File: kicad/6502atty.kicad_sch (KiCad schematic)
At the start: 30 parts, among them J10 Conn_01x04_Pin, J11 Conn_01x03_Pin, J12 Conn_01x02_Pin, J2 Conn_01x02_Pin, J8 Conn_01x03_Pin, U6 27C128, U7 KM62256CLP

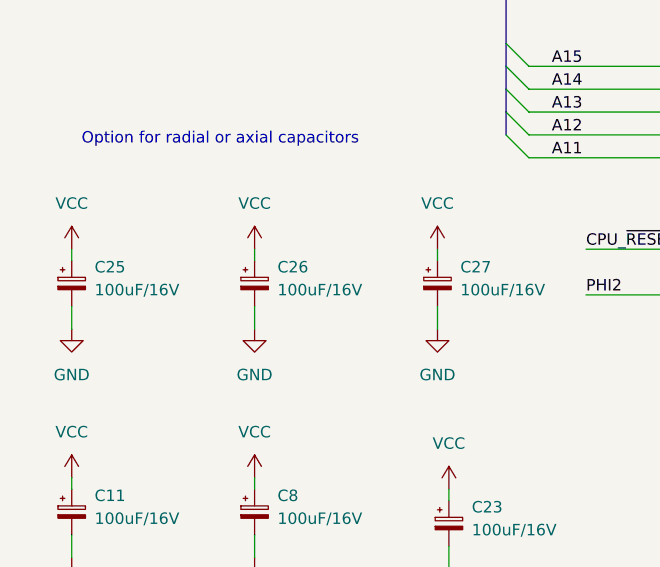
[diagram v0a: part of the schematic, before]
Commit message: pcb: move around stuff to make pcb smaller
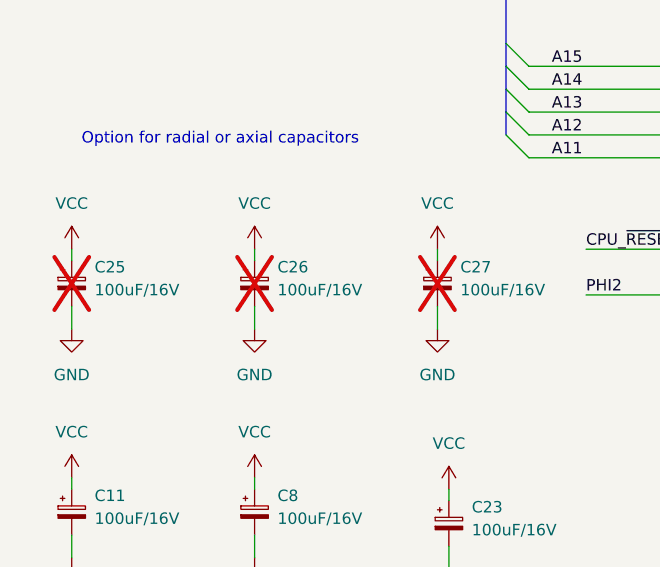
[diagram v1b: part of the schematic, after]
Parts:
- C25, C26, C27: now not fitted
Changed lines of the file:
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@@
 		(in_bom yes)
 		(on_board yes)
-		(dnp no)
+		(dnp yes)
 		(fields_autoplaced yes)
 		(property "Reference" "C26"
@@
 		(in_bom yes)
 		(on_board yes)
-		(dnp no)
+		(dnp yes)
 		(fields_autoplaced yes)
 		(property "Reference" "C27"
@@
 		(in_bom yes)
 		(on_board yes)
-		(dnp no)
+		(dnp yes)
 		(fields_autoplaced yes)
 		(property "Reference" "C25"

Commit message: start of rev3, reduce x-size, leds consistent
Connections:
- net GND: now also R37.2; no longer D2.1 (K)
- net VCC: now also D2.2 (A); no longer R37.1
- new net: D2.1 (K), R37.1
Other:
- moved on the sheet: R37
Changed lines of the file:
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@@
 	(wire
 		(pts
+			(xy 234.95 105.41) (xy 234.95 104.14)
+		)
+		(stroke
+			(width 0)
+			(type default)
+		)
+	)
+	(wire
+		(pts
 			(xy 189.23 53.34) (xy 198.12 53.34)
 		)
@@
 	(wire
 		(pts
+			(xy 234.95 113.03) (xy 234.95 115.57)
+		)
+		(stroke
+			(width 0)
+			(type default)
+		)
+	)
+	(wire
+		(pts
 			(xy 260.35 34.29) (xy 260.35 33.02)
 		)
@@
 		)
 	)
+	(wire
+		(pts
+			(xy 234.95 90.17) (xy 234.95 99.06)
+		)
+		(stroke
+			(width 0)
+			(type default)
+		)
+	)
 	(bus
 		(pts
@@
 		)
 	)
-	(wire
-		(pts
-			(xy 234.95 97.79) (xy 234.95 99.06)
-		)
-		(stroke
-			(width 0)
-			(type default)
-		)
-	)
 	(bus
 		(pts
@@
 	(wire
 		(pts
-			(xy 234.95 104.14) (xy 234.95 106.68)
-		)
-		(stroke
-			(width 0)
-			(type default)
-		)
-	)
-	(wire
-		(pts
 			(xy 24.13 66.04) (xy 38.1 66.04)
 		)
@@
 	(symbol
 		(lib_id "power:GND")
-		(at 234.95 106.68 0)
+		(at 234.95 115.57 0)
 		(unit 1)
 		(exclude_from_sim no)
@@
 		(dnp no)
 		(property "Reference" "#PWR0102"
-			(at 234.95 113.03 0)
+			(at 234.95 121.92 0)
 			(effects
 				(font
@@
 		)
 		(property "Value" "GND"
-			(at 234.95 111.76 0)
+			(at 234.95 120.65 0)
 			(effects
 				(font
@@
 		)
 		(property "Footprint" ""
-			(at 234.95 106.68 0)
+			(at 234.95 115.57 0)
 			(effects
 				(font
@@
 		)
 		(property "Datasheet" ""
-			(at 234.95 106.68 0)
+			(at 234.95 115.57 0)
 			(effects
 				(font
@@
 		)
 		(property "Description" "Power symbol creates a global label with name \"GND\" , ground"
-			(at 234.95 106.68 0)
+			(at 234.95 115.57 0)
 			(effects
 				(font
@@
 	(symbol
 		(lib_id "Device:R")
-		(at 234.95 93.98 0)
+		(at 234.95 109.22 0)
 		(unit 1)
 		(exclude_from_sim no)
@@
 		(fields_autoplaced yes)
 		(property "Reference" "R37"
-			(at 237.49 92.7099 0)
+			(at 237.49 107.9499 0)
 			(effects
 				(font
@@
 		)
 		(property "Value" "1K"
-			(at 237.49 95.2499 0)
+			(at 237.49 110.4899 0)
 			(effects
 				(font
@@
 		)
 		(property "Footprint" "Resistor_THT:R_Axial_DIN0207_L6.3mm_D2.5mm_P10.16mm_Horizontal"
-			(at 233.172 93.98 90)
+			(at 233.172 109.22 90)
 			(effects
 				(font
@@
 		)
 		(property "Datasheet" "~"
-			(at 234.95 93.98 0)
+			(at 234.95 109.22 0)
 			(effects
 				(font
@@
 		)
 		(property "Description" "Resistor"
-			(at 234.95 93.98 0)
+			(at 234.95 109.22 0)
 			(effects
 				(font

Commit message: updates for moving pcb stuff around
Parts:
- removed J8: Conn_01x03_Pin, Connector_PinHeader_2.54mm:PinHeader_1x03_P2.54mm_Vertical, symbol Connector:Conn_01x03_Pin
- added JP1: A13-Sel, symbol Jumper:SolderJumper_3_Bridged12
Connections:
- net A13: now also JP1.1 (A)
- net GND: now also JP1.3 (B)
- net ROM_A13: now also JP1.2 (C)
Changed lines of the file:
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@@
 	)
 	(bus_entry
-		(at 152.4 104.14)
+		(at 152.4 92.71)
 		(size -2.54 2.54)
 		(stroke
@@
 		)
 	)
+	(bus
+		(pts
+			(xy 152.4 97.79) (xy 152.4 100.33)
+		)
+		(stroke
+			(width 0)
+			(type default)
+		)
+	)
 	(wire
 		(pts
@@
 		)
 	)
-	(bus
-		(pts
-			(xy 152.4 95.25) (xy 152.4 97.79)
-		)
-		(stroke
-			(width 0)
-			(type default)
-		)
-	)
 	(wire
 		(pts
@@
 		)
 	)
-	(bus
-		(pts
-			(xy 152.4 97.79) (xy 152.4 100.33)
-		)
-		(stroke
-			(width 0)
-			(type default)
-		)
-	)
 	(wire
 		(pts
@@
 	(wire
 		(pts
-			(xy 148.59 130.81) (xy 148.59 109.22)
+			(xy 148.59 130.81) (xy 148.59 104.14)
 		)
 		(stroke
@@
 		)
 	)
+	(wire
+		(pts
+			(xy 142.24 95.25) (xy 149.86 95.25)
+		)
+		(stroke
+			(width 0)
+			(type default)
+		)
+	)
 	(bus
 		(pts
@@
 		)
 	)
-	(bus
-		(pts
-			(xy 152.4 104.14) (xy 152.4 105.41)
-		)
-		(stroke
-			(width 0)
-			(type default)
-		)
-	)
 	(wire
 		(pts
@@
 	(wire
 		(pts
+			(xy 142.24 110.49) (xy 142.24 109.22)
+		)
+		(stroke
+			(width 0)
+			(type default)
+		)
+	)
+	(wire
+		(pts
 			(xy 39.37 187.96) (xy 39.37 185.42)
 		)
@@
 	(bus
 		(pts
+			(xy 152.4 100.33) (xy 152.4 102.87)
+		)
+		(stroke
+			(width 0)
+			(type default)
+		)
+	)
+	(bus
+		(pts
 			(xy 152.4 50.8) (xy 152.4 53.34)
 		)
@@
 	(bus
 		(pts
-			(xy 152.4 100.33) (xy 152.4 102.87)
+			(xy 152.4 95.25) (xy 152.4 97.79)
+		)
+		(stroke
+			(width 0)
+			(type default)
+		)
+	)
+	(bus
+		(pts
+			(xy 152.4 92.71) (xy 152.4 95.25)
 		)
 		(stroke
@@
 	(wire
 		(pts
-			(xy 146.05 106.68) (xy 149.86 106.68)
+			(xy 78.74 71.12) (xy 90.17 71.12)
 		)
 		(stroke
@@
 	(wire
 		(pts
-			(xy 78.74 71.12) (xy 90.17 71.12)
+			(xy 25.4 53.34) (xy 38.1 53.34)
 		)
 		(stroke
@@
 	(wire
 		(pts
-			(xy 25.4 53.34) (xy 38.1 53.34)
+			(xy 259.08 104.14) (xy 259.08 118.11)
 		)
 		(stroke
@@
 	(wire
 		(pts
-			(xy 259.08 104.14) (xy 259.08 118.11)
+			(xy 19.05 187.96) (xy 19.05 185.42)
 		)
 		(stroke
@@
 	(wire
 		(pts
-			(xy 19.05 187.96) (xy 19.05 185.42)
+			(xy 114.3 138.43) (xy 124.46 138.43)
 		)
 		(stroke
@@
 	(wire
 		(pts
-			(xy 114.3 138.43) (xy 124.46 138.43)
+			(xy 154.94 128.27) (xy 166.37 128.27)
 		)
 		(stroke
@@
 	(wire
 		(pts
-			(xy 154.94 128.27) (xy 166.37 128.27)
+			(xy 142.24 95.25) (xy 142.24 99.06)
 		)
 		(stroke
@@
 	(wire
 		(pts
-			(xy 148.59 109.22) (xy 146.05 109.22)
+			(xy 148.59 104.14) (xy 146.05 104.14)
 		)
 		(stroke
@@
 	(bus
 		(pts
+			(xy 152.4 102.87) (xy 152.4 105.41)
+		)
+		(stroke
+			(width 0)
+			(type default)
+		)
+	)
+	(bus
+		(pts
 			(xy 152.4 27.94) (xy 152.4 35.56)
 		)
@@
 		)
 	)
-	(bus
-		(pts
-			(xy 152.4 102.87) (xy 152.4 104.14)
-		)
-		(stroke
-			(width 0)
-			(type default)
-		)
-	)
 	(wire
 		(pts
@@
 	(bus
 		(pts
-			(xy 152.4 71.12) (xy 152.4 95.25)
+			(xy 152.4 71.12) (xy 152.4 92.71)
 		)
 		(stroke
@@
 	)
 	(label "A13"
-		(at 146.05 106.68 0)
+		(at 146.05 95.25 0)
 		(effects
 			(font
@@
 	)
 	(symbol
-		(lib_id "Connector:Conn_01x03_Pin")
-		(at 140.97 109.22 0)
-		(unit 1)
-		(exclude_from_sim no)
-		(in_bom yes)
-		(on_board yes)
-		(dnp no)
-		(property "Reference" "J8"
-			(at 141.605 101.6 0)
-			(effects
-				(font
-					(size 1.27 1.27)
-				)
-			)
-		)
-		(property "Value" "Conn_01x03_Pin"
-			(at 138.938 106.68 90)
-			(effects
-				(font
-					(size 1.27 1.27)
-				)
-			)
-		)
-		(property "Footprint" "Connector_PinHeader_2.54mm:PinHeader_1x03_P2.54mm_Vertical"
-			(at 140.97 109.22 0)
-			(effects
-				(font
-					(size 1.27 1.27)
-				)
-				(hide yes)
-			)
-		)
-		(property "Datasheet" "~"
-			(at 140.97 109.22 0)
-			(effects
-				(font
-					(size 1.27 1.27)
-				)
-				(hide yes)
-			)
-		)
-		(property "Description" "Generic connector, single row, 01x03, script generated"
-			(at 140.97 109.22 0)
-			(effects
-				(font
-					(size 1.27 1.27)
-				)
-				(hide yes)
-			)
-		)
-		(pin "1"
-		)
-		(pin "3"
-		)
-		(pin "2"
-		)
-		(instances
-			(project ""
-				(path "/f612fa92-d5fa-4cb5-a666-c1c24e7cbb30"
-					(reference "J8")
-					(unit 1)
-				)
-			)
-		)
-	)
-	(symbol
 		(lib_id "power:VCC")
 		(at 259.08 90.17 0)
@@
 	(symbol
 		(lib_id "power:GND")
-		(at 146.05 111.76 0)
+		(at 142.24 110.49 0)
 		(unit 1)
 		(exclude_from_sim no)
@@
 		(dnp no)
 		(property "Reference" "#PWR039"
-			(at 146.05 118.11 0)
+			(at 142.24 116.84 0)
 			(effects
 				(font
@@
 		)
 		(property "Value" "GND"
-			(at 146.05 116.84 0)
+			(at 142.24 115.57 0)
 			(effects
 				(font
@@
 		)
 		(property "Footprint" ""
-			(at 146.05 111.76 0)
+			(at 142.24 110.49 0)
 			(effects
 				(font
@@
 		)
 		(property "Datasheet" ""
-			(at 146.05 111.76 0)
+			(at 142.24 110.49 0)
 			(effects
 				(font
@@
 		)
 		(property "Description" "Power symbol creates a global label with name \"GND\" , ground"
-			(at 146.05 111.76 0)
+			(at 142.24 110.49 0)
 			(effects
 				(font
@@
 					(unit 1)
 				)
+			)
+		)
+	)
+	(symbol
+		(lib_id "Jumper:SolderJumper_3_Bridged12")
+		(at 142.24 104.14 90)
+		(mirror x)
+		(unit 1)
+		(exclude_from_sim no)
+		(in_bom no)
+		(on_board yes)
+		(dnp no)
+		(property "Reference" "JP1"
+			(at 146.812 100.584 90)
+			(effects
+				(font
+					(size 1.27 1.27)
+				)
+				(justify left)
+			)
+		)
+		(property "Value" "A13-Sel"
+			(at 138.43 99.822 0)
+			(effects
+				(font
+					(size 1.27 1.27)
+				)
+				(justify left)
+			)
+		)
+		(property "Footprint" ""
+			(at 142.24 104.14 0)
+			(effects
+				(font
+					(size 1.27 1.27)
+				)
+				(hide yes)
+			)
+		)
+		(property "Datasheet" "~"
+			(at 142.24 104.14 0)
+			(effects
+				(font
+					(size 1.27 1.27)
+				)
+				(hide yes)
+			)
+		)
+		(property "Description" "3-pole Solder Jumper, pins 1+2 closed/bridged"
+			(at 142.24 104.14 0)
+			(effects
+				(font
+					(size 1.27 1.27)
+				)
+				(hide yes)
+			)
+		)
+		(pin "2"
+		)
+		(pin "1"
+		)
+		(pin "3"
+		)
+		(instances
+			(project ""
+				(path "/f612fa92-d5fa-4cb5-a666-c1c24e7cbb30"
+					(reference "JP1")
+					(unit 1)
+				)

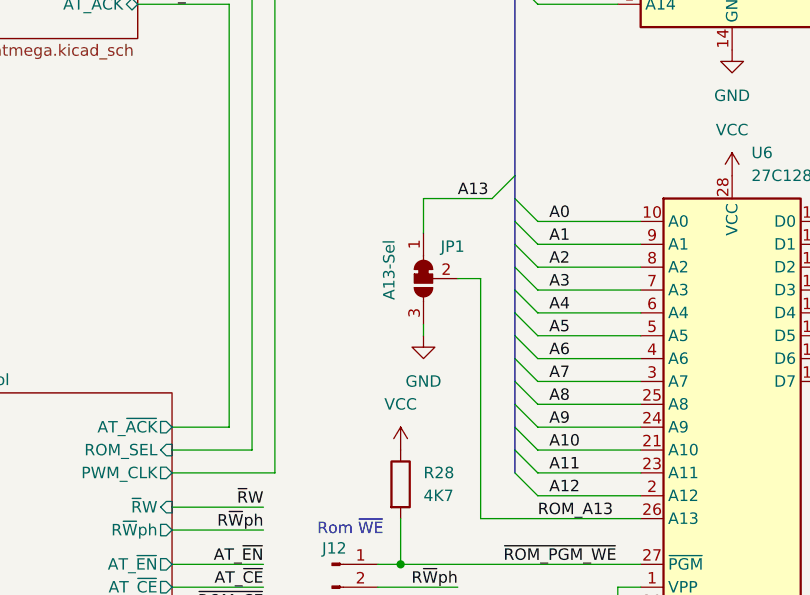
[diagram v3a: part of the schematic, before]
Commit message: kicad: routing and board updates
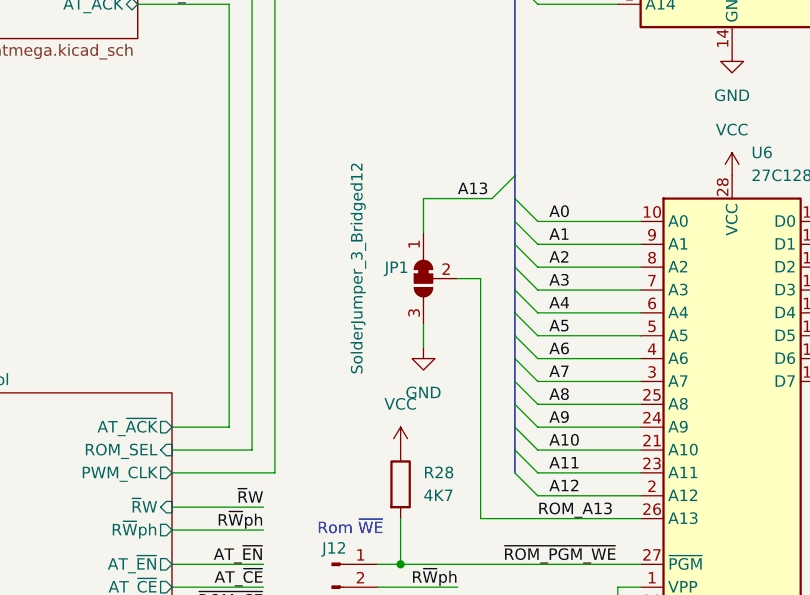
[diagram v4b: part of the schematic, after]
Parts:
- JP1: value A13-Sel -> SolderJumper_3_Bridged12; footprint (none) -> Jumper:SolderJumper-3_P1.3mm_Bridged12_Pad1.0x1.5mm_NumberLabels
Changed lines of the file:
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@@
 	(wire
 		(pts
+			(xy 142.24 109.22) (xy 142.24 111.76)
+		)
+		(stroke
+			(width 0)
+			(type default)
+		)
+	)
+	(wire
+		(pts
 			(xy 76.2 158.75) (xy 90.17 158.75)
 		)
@@
 	(wire
 		(pts
-			(xy 142.24 110.49) (xy 142.24 109.22)
-		)
-		(stroke
-			(width 0)
-			(type default)
-		)
-	)
-	(wire
-		(pts
 			(xy 39.37 187.96) (xy 39.37 185.42)
 		)
@@
 	(symbol
 		(lib_id "power:GND")
-		(at 142.24 110.49 0)
+		(at 142.24 111.76 0)
 		(unit 1)
 		(exclude_from_sim no)
@@
 		(dnp no)
 		(property "Reference" "#PWR039"
-			(at 142.24 116.84 0)
+			(at 142.24 118.11 0)
 			(effects
 				(font
@@
 		)
 		(property "Value" "GND"
-			(at 142.24 115.57 0)
+			(at 142.24 116.84 0)
 			(effects
 				(font
@@
 		)
 		(property "Footprint" ""
-			(at 142.24 110.49 0)
+			(at 142.24 111.76 0)
 			(effects
 				(font
@@
 		)
 		(property "Datasheet" ""
-			(at 142.24 110.49 0)
+			(at 142.24 111.76 0)
 			(effects
 				(font
@@
 		)
 		(property "Description" "Power symbol creates a global label with name \"GND\" , ground"
-			(at 142.24 110.49 0)
+			(at 142.24 111.76 0)
 			(effects
 				(font
@@
 		(dnp no)
 		(property "Reference" "JP1"
-			(at 146.812 100.584 90)
+			(at 140.5891 102.9278 90)
 			(effects
 				(font
@@
 			)
 		)
-		(property "Value" "A13-Sel"
-			(at 138.43 99.822 0)
+		(property "Value" "SolderJumper_3_Bridged12"
+			(at 134.874 91.186 0)
 			(effects
 				(font
@@
 			)
 		)
-		(property "Footprint" ""
+		(property "Footprint" "Jumper:SolderJumper-3_P1.3mm_Bridged12_Pad1.0x1.5mm_NumberLabels"
 			(at 142.24 104.14 0)
 			(effects

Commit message: updated to use 74x574 for input, then drc fixes
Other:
- sheet IO ports: added IOCLK; removed none
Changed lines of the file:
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@@
 	(wire
 		(pts
+			(xy 223.52 55.88) (xy 231.14 55.88)
+		)
+		(stroke
+			(width 0)
+			(type default)
+		)
+	)
+	(wire
+		(pts
 			(xy 60.96 71.12) (xy 78.74 71.12)
 		)
@@
 		)
 	)
+	(label "PHI2"
+		(at 223.52 55.88 0)
+		(effects
+			(font
+				(size 1.27 1.27)
+			)
+			(justify left bottom)
+		)
+	)
 	(symbol
 		(lib_id "Device:R")
@@
 			(effects
 				(font
+					(size 1.27 1.27)
+				)
+				(justify left)
+			)
+		)
+		(pin "IOCLK" input
+			(at 231.14 55.88 180)
+			(effects
+				(font
